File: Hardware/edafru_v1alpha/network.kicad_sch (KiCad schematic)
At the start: 9 parts, among them U6 SN65HVD1050D

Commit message: PCB is developing...
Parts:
- removed D4: SZNUP2105L, Package_TO_SOT_SMD:SOT-23, symbol Power_Protection:SZNUP2105L
- removed R44: 47K, Resistor_SMD:R_0603_1608Metric_Pad0.98x0.95mm_HandSolder, symbol Device:R
- removed R45, R47: 59R9, Resistor_SMD:R_0603_1608Metric_Pad0.98x0.95mm_HandSolder, symbol Device:R
- removed R46, R48: 0R, Resistor_SMD:R_0603_1608Metric_Pad0.98x0.95mm_HandSolder, symbol Device:R
- removed U6: SN65HVD1050D, Package_SO:SOIC-8_3.9x4.9mm_P1.27mm, symbol Interface_CAN_LIN:SN65HVD1050D
- added C29: 100nF, Capacitor_SMD:C_0603_1608Metric_Pad1.08x0.95mm_HandSolder, symbol Device:C
- added D4: 1N4148W, Diode_SMD:D_SOD-123, symbol Diode:1N4148W
- added D5, D6: SZNUP2105L, Package_TO_SOT_SMD:SOT-23, symbol Power_Protection:SZNUP2105L
- added R50, R51, R52, R55: 47K, Resistor_SMD:R_0603_1608Metric_Pad0.98x0.95mm_HandSolder, symbol Device:R
- added R53, R57, R59, R60: 0R, Resistor_SMD:R_0603_1608Metric_Pad0.98x0.95mm_HandSolder, symbol Device:R
- added R54: 1K, Resistor_SMD:R_0603_1608Metric_Pad0.98x0.95mm_HandSolder, symbol Device:R
- added R56, R58: 59R9, Resistor_SMD:R_0603_1608Metric_Pad0.98x0.95mm_HandSolder, symbol Device:R
- added U6: TJA1021T, Package_SO:SOIC-8_3.9x4.9mm_P1.27mm, symbol Interface_CAN_LIN:TJA1021T
- added U7: SN65HVD1050D, Package_SO:SOIC-8_3.9x4.9mm_P1.27mm, symbol Interface_CAN_LIN:SN65HVD1050D
- R49: value 0R -> 47K
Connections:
- net CAND_N: now also R56.2, R60.2, U7.6 (CANL); no longer R49.2
- net CAND_P: now also R58.2, R59.2, U7.7 (CANH)
- net CAN_D_N: now also U7.4 (RXD)
- net CAN_D_P: now also U7.1 (TXD)
- net CAN_H: now also D6.1 (K), R59.1
- net CAN_L: now also D6.2 (K), R60.1; no longer R49.1
- net CAN_SLEEP: now also R55.1, U7.8 (S)
- net GND: now also C29.2, D5.3 (A), D6.3 (A), R55.2, U6.5 (GND), U7.2 (GND)
- net VCC: now also R49.2, R50.2, R51.2, R52.2, U7.3 (VCC)
- net LIN_BUS: now reaches C28.1
- net LIN_BUS: now also D5.2 (K), R53.1
- new net: R53.2, U6.6 (LIN)
- new net: D4.1 (K), R54.2
- new net: R57.1, U7.5 (VREF)
- new net: C29.1, R56.1, R57.2, R58.1
- new net: R52.1, U6.3 (~{WAKE})
- new net: D4.2 (A), U6.8 (INH)
- new net +12P: U6.7 (VBAT)
- new net LIN_D_RX: R49.1, U6.1 (RXD)
- new net LIN_D_TX: R50.1, U6.4 (TXD)
- new net LIN_INH: D5.1 (K), R54.1
- new net LIN_SLP_N: R51.1, U6.2 (~{SLP})
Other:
- note added: "LIN"

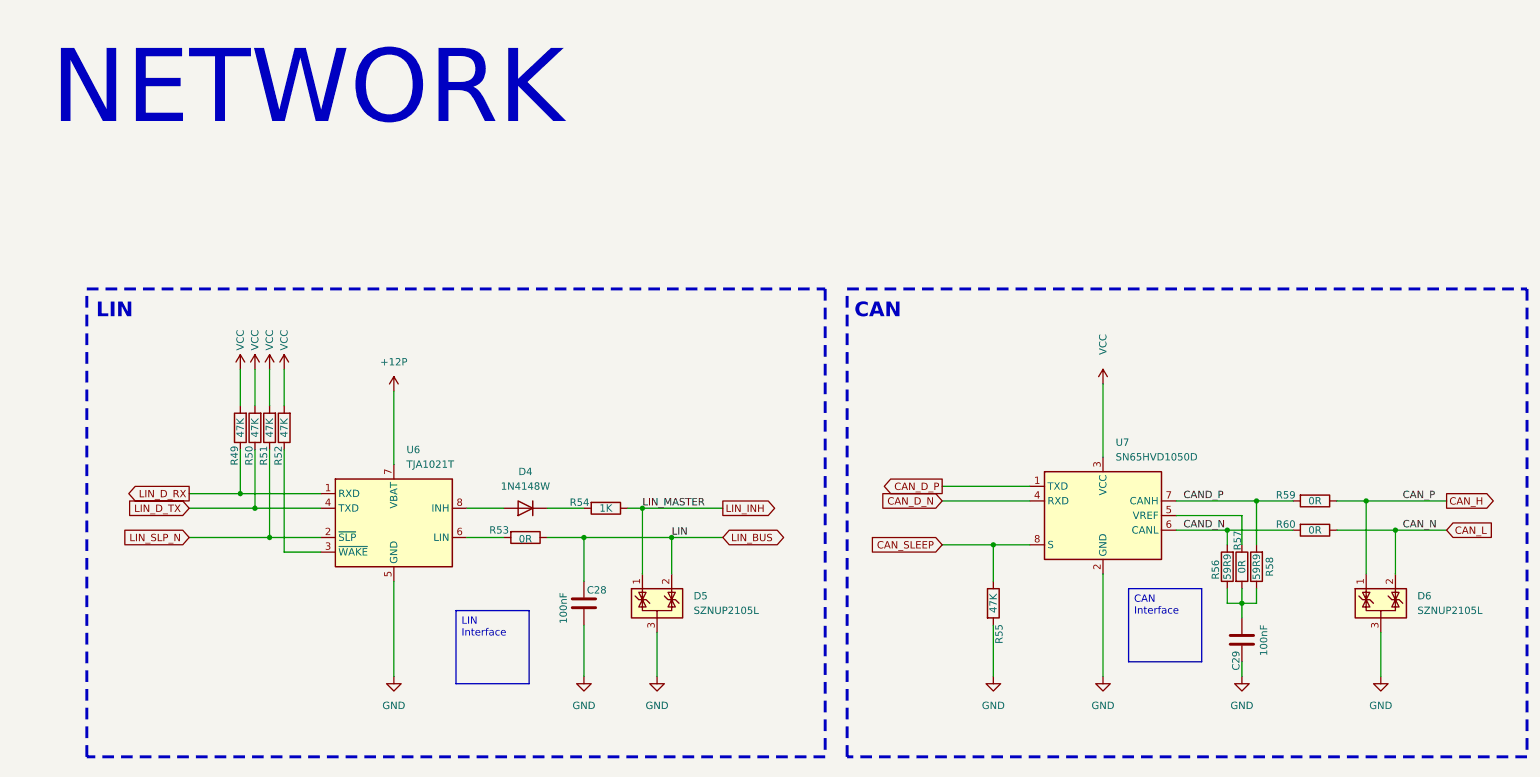
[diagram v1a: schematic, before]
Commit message: developement is stopped depend on new EDVDU.
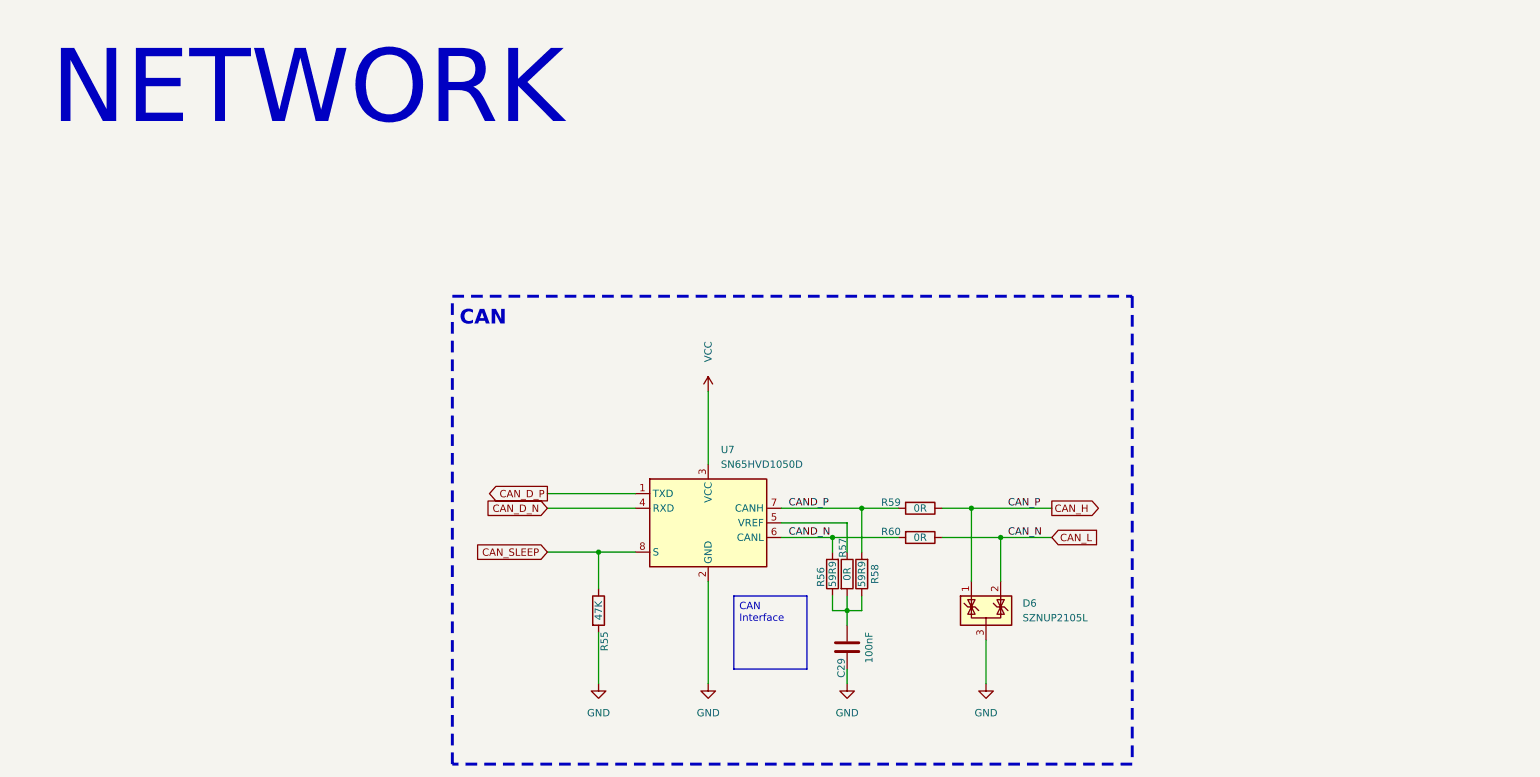
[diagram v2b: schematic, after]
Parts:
- removed C28: 100nF, Capacitor_SMD:C_0603_1608Metric_Pad1.08x0.95mm_HandSolder, symbol Device:C
- removed D4: 1N4148W, Diode_SMD:D_SOD-123, symbol Diode:1N4148W
- removed D5: SZNUP2105L, Package_TO_SOT_SMD:SOT-23, symbol Power_Protection:SZNUP2105L
- removed R49, R50, R51, R52: 47K, Resistor_SMD:R_0603_1608Metric_Pad0.98x0.95mm_HandSolder, symbol Device:R
- removed R53: 0R, Resistor_SMD:R_0603_1608Metric_Pad0.98x0.95mm_HandSolder, symbol Device:R
- removed R54: 1K, Resistor_SMD:R_0603_1608Metric_Pad0.98x0.95mm_HandSolder, symbol Device:R
- removed U6: TJA1021T, Package_SO:SOIC-8_3.9x4.9mm_P1.27mm, symbol Interface_CAN_LIN:TJA1021T
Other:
- note removed: "LIN"
- moved on the sheet: C29, D6, R55, R56, R57, R58, R59, R60, U7
